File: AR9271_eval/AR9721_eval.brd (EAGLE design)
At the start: 160 x 100 mm, 125 parts, among them J1 UJ2-MIBH2-4-SMT-TR, J3 HTST-110-01-XX-DV, J7 132134-15, J8 132134-15, U1 U-ATHEROS-AR9271, U2 AT24C04C-XHM-T, U3 LT3080EQPBF, U4 LT3080EQPBF, U5 LT3080EQPBF, U6 LT3080EQPBF, Y1 ECS-400-10-36-CKY-TR

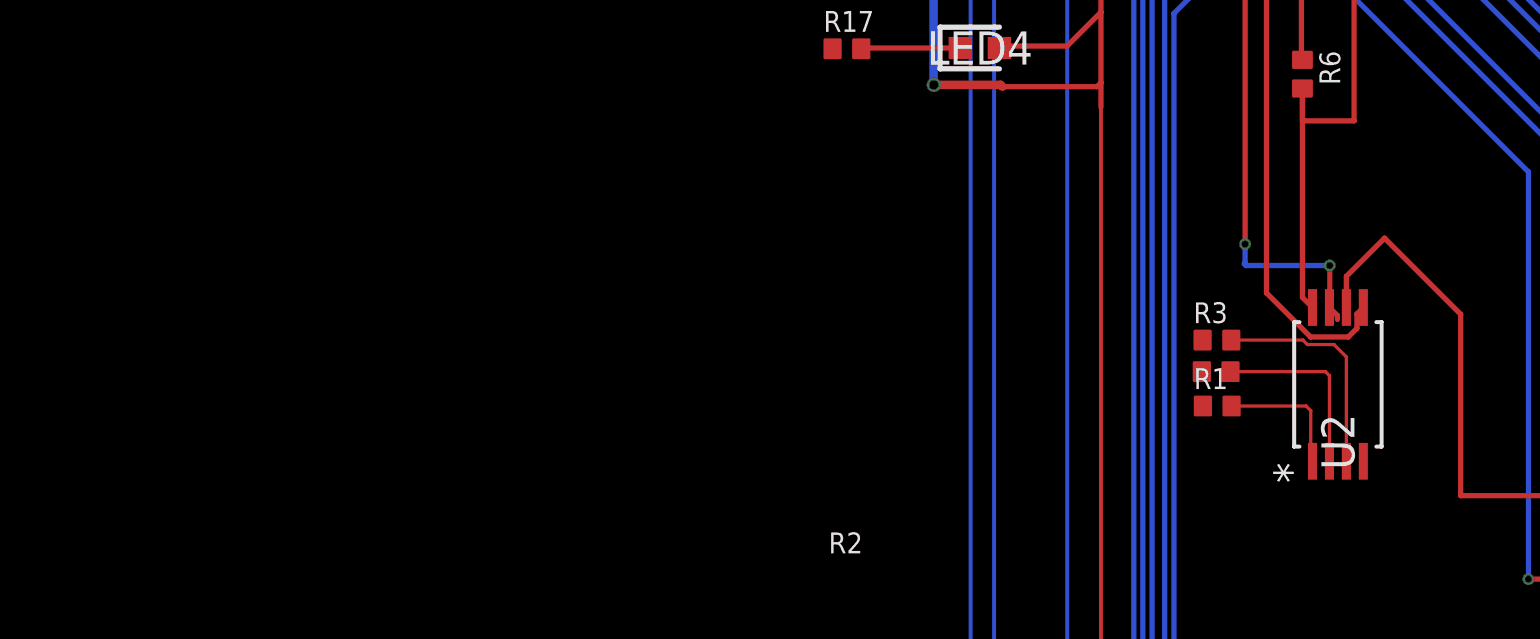
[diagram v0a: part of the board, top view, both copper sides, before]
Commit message: BRD and SCH now back in sync
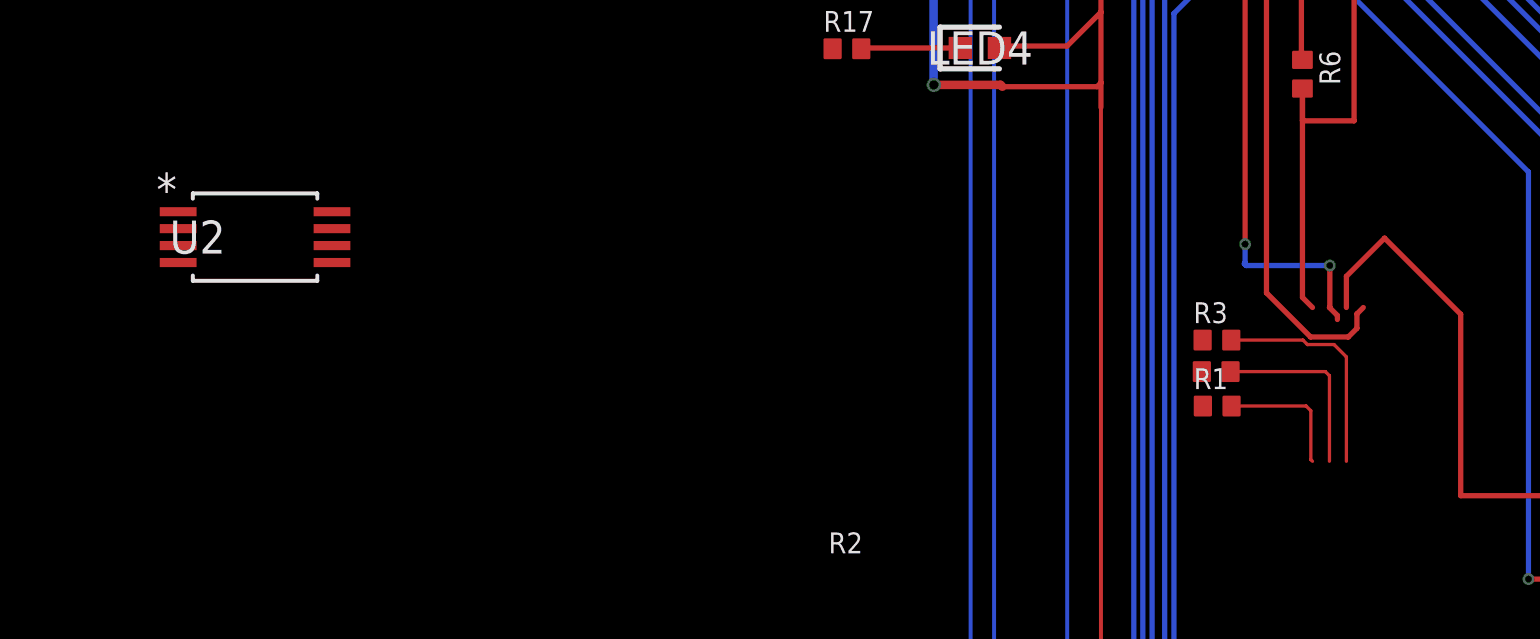
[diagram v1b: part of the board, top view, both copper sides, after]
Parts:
- U2: device AT24C04_TSSOP:8X -> U-Generic-AT24C04-EEPROM-I2C-4Kb-TSSOP:8X
- moved U2 41.9 mm to (44.1, 30.4), turned to 0 degrees

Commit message: Add files via upload
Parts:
- moved C39 99.7 mm to (32.0, 28.9)
- moved C27 96.9 mm to (24.7, 30.5)
- moved C28 92.2 mm to (25.8, 30.4)
- moved C37 86.3 mm to (22.2, 33.8), turned to 180 degrees
- moved C38 83.1 mm to (26.8, 28.8), turned to 180 degrees
- moved C36 80.9 mm to (22.2, 35.6), turned to 180 degrees
- moved C29 78.7 mm to (36.6, 29.3)
- moved C35 75.7 mm to (24.2, 44.4), turned to 180 degrees
- moved C33 75.1 mm to (24.2, 43.4), turned to 180 degrees
- moved C30 73.0 mm to (38.2, 29.3)
- moved C34 73.0 mm to (26.7, 43.3), turned to 180 degrees
- moved C40 66.2 mm to (43.0, 37.0)
- moved C50 61.5 mm to (63.7, 57.4)
- moved C41 60.7 mm to (29.1, 44.3)
- moved C31 60.5 mm to (42.1, 40.2), turned to 90 degrees
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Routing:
- net 3V3_D: track 202.7 -> 101.1 mm, vias 22 -> 15
- net LDO_IN: track 141.5 -> 90.0 mm, vias 11 -> 6
- net 1V2_A: track 91.9 -> 41.2 mm, vias 5 -> 3
- net N$25: track 53.2 -> 21.0 mm, vias 2 -> 0
- net N$3: track 57.8 -> 32.4 mm
- net GPIO11: track 114.3 -> 94.0 mm
- net N$23: track 23.2 -> 3.28 mm, vias 3 -> 0
- net RST_L: track 57.8 -> 41.0 mm
- net GPIO6: track 95.5 -> 78.8 mm
- net GPIO8: track 99.5 -> 82.7 mm
- net GPIO7: track 97.5 -> 80.7 mm
- net SWCOM1: track 55.9 -> 39.6 mm
- net GPIO5: track 93.7 -> 77.7 mm, vias 3 -> 2
- net SWCOM0: track 61.1 -> 45.1 mm
- net SWCOM2: track 60.7 -> 46.0 mm
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- removed copper zone on layer 15, net N$23
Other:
- board size 160 x 100 mm -> 105.7 x 84.6 mm

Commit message: Add files via upload
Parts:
- moved C46 28.8 mm to (61.8, 56.1)
- moved LED1 28.7 mm to (2.04, 7.56), turned to 270 degrees
- moved R34 28.6 mm to (55.2, 55.2)
- moved C22 28.4 mm to (15.4, 55.7)
- moved U4 28.4 mm to (58.5, 72.4)
- moved U6 28.4 mm to (44.5, 72.0)
- moved C23 28.4 mm to (12.3, 59.8)
- moved C47 28.4 mm to (30.6, 55.5)
- moved C48 28.4 mm to (28.0, 58.1)
- moved R33 28.4 mm to (25.5, 55.5)
- moved U5 28.4 mm to (30.6, 72.0)
- moved C1 28.4 mm to (33.1, 55.6)
- moved C24 28.4 mm to (19.2, 54.8)
- moved C49 28.4 mm to (48.3, 57.0)
- moved R27 28.4 mm to (12.3, 61.0)
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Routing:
- net LDO_IN: track 90.0 -> 122.6 mm, vias 6 -> 23
- net 1V2_D: track 90.0 -> 66.1 mm, vias 2 -> 12
- net USB_DM: track 83.4 -> 62.8 mm
- net N$32: track 5.22 -> 22.4 mm
- net N$25: track 21.0 -> 4.03 mm
- net 1V2_A: track 41.2 -> 24.9 mm, vias 3 -> 12
- net TDO: track 16.9 -> 32.4 mm
- net TCK: track 45.9 -> 60.9 mm
- net TDI: track 36.7 -> 51.6 mm
- net TMS: track 34.9 -> 48.8 mm
- net RST_L: track 41.0 -> 54.4 mm
- net 3V3_D: track 101.1 -> 114.1 mm, vias 15 -> 20
- net N$47: track 26.2 -> 14.2 mm, vias 4 -> 6
- net RCV_IN: track 5.29 -> 16.4 mm
- net N$37: track 22.0 -> 13.5 mm, vias 3 -> 9
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- added copper zone on layer 16, net GND
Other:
- board size 105.7 x 84.6 mm -> 98.9 x 78.9 mm

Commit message: Add files via upload
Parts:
- moved J4 5.20 mm to (86.1, 3.21)
- moved J6 5.20 mm to (82.3, 3.21)
- moved LED10 5.20 mm to (74.7, 8.29)
- moved LED11 5.20 mm to (77.2, 8.30)
- moved LED12 5.20 mm to (79.7, 8.29)
- moved LED6 5.20 mm to (64.5, 8.29)
- moved LED8 5.20 mm to (69.6, 8.28)
- moved R19 5.20 mm to (64.5, 12.1)
- moved R21 5.20 mm to (69.6, 12.1)
- moved R23 5.20 mm to (74.7, 12.1)
- moved R24 5.20 mm to (77.2, 12.1)
- moved R25 5.20 mm to (79.7, 12.1)
- moved LED5 5.20 mm to (62.0, 8.29)
- moved R18 5.20 mm to (62.0, 12.1)
- moved LED7 5.20 mm to (67.0, 8.29)
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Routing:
- net GPIO9: track 79.7 -> 74.5 mm
- net GPIO8: track 78.7 -> 73.5 mm
- net GPIO13: track 71.7 -> 66.5 mm
- net GPIO10: track 76.7 -> 71.5 mm
- net GPIO14: track 65.1 -> 59.9 mm
- net GPIO7: track 76.7 -> 71.5 mm
- net GPIO6: track 74.8 -> 69.6 mm
- net GPIO5: track 73.7 -> 68.5 mm
- net GPIO15: track 74.9 -> 69.7 mm
- net GPIO11: track 89.6 -> 84.4 mm
- net 3V3_A: track 63.9 -> 58.8 mm, vias 11 -> 10
- net TDO: track 32.4 -> 28.4 mm
- net USB_DM: track 62.8 -> 58.9 mm
- net USB_DP: track 68.3 -> 64.4 mm
- net LDO_IN: track 122.6 -> 118.7 mm
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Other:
- board size 98.9 x 78.9 mm -> 94.2 x 78.9 mm

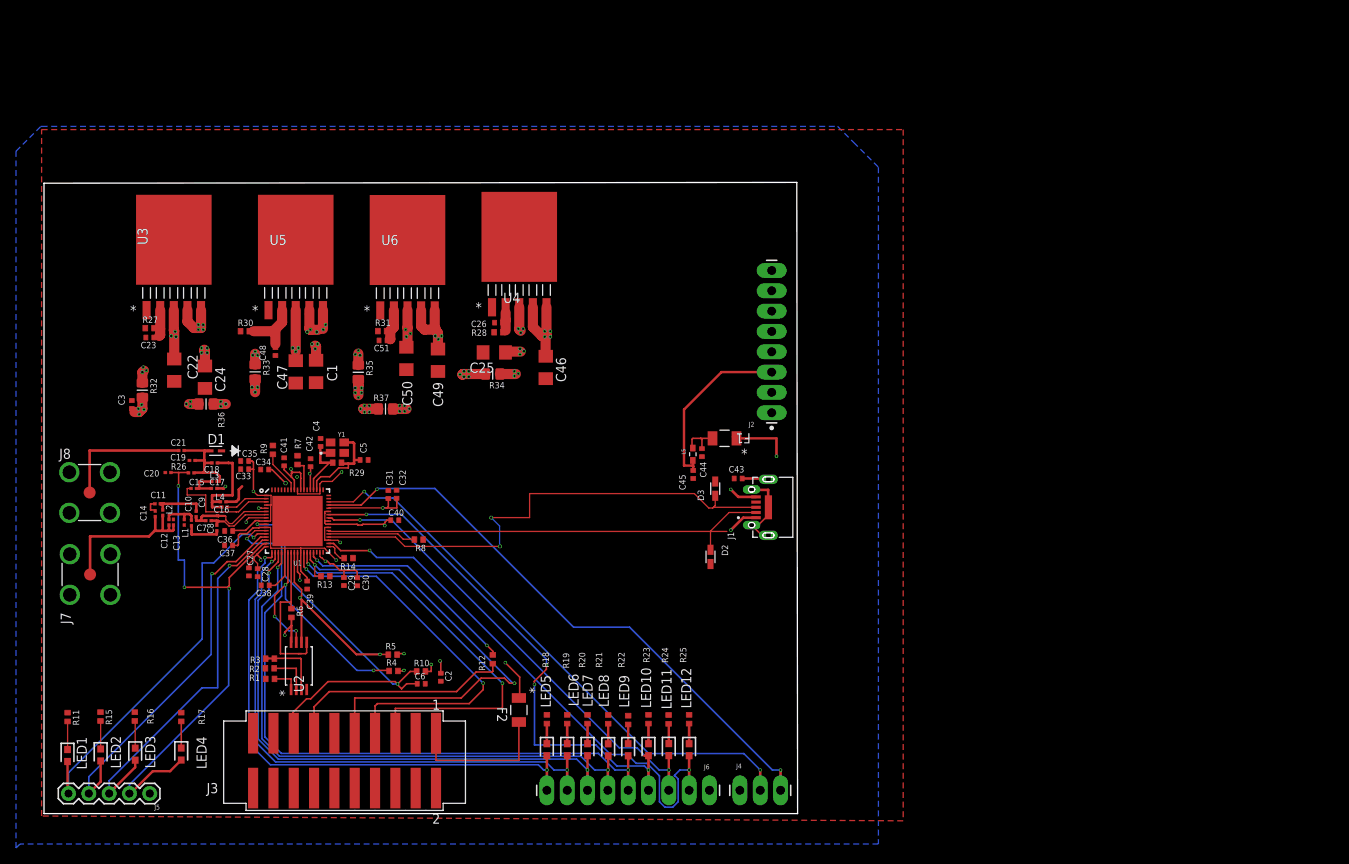
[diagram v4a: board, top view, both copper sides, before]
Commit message: Beginning of OCD cleanup; started with USB lines, worked on RF layout grouping, moved to power planes.
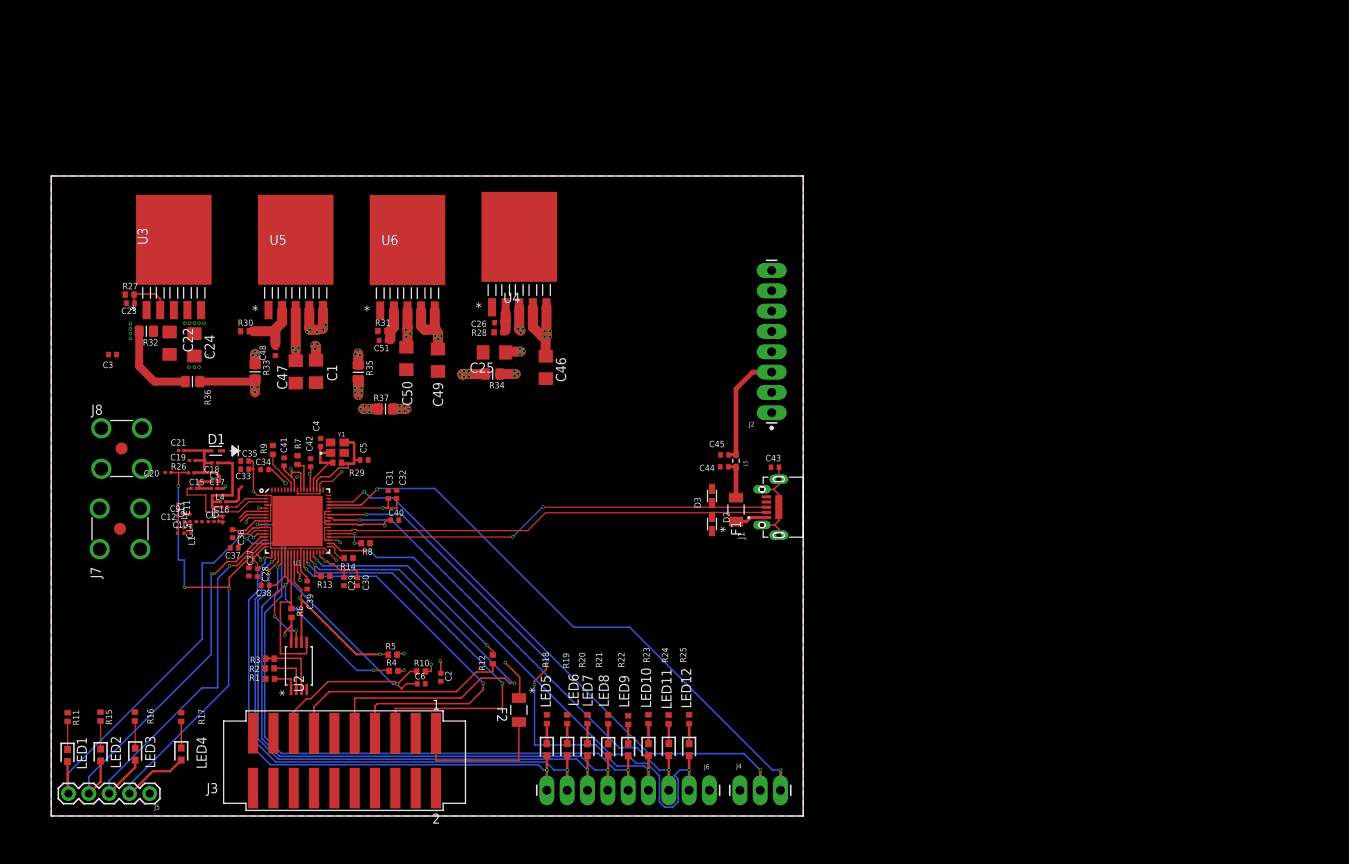
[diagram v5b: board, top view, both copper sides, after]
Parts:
- moved F1 9.02 mm to (85.6, 38.3), turned to 90 degrees
- moved R32 7.39 mm to (11.9, 60.6), turned to 180 degrees
- moved J7 6.83 mm to (8.60, 35.9)
- moved J8 6.80 mm to (8.80, 45.9)
- moved C3 6.70 mm to (7.67, 57.7), turned to 180 degrees
- moved R8 6.67 mm to (39.3, 34.1), turned to 180 degrees
- moved L5 5.46 mm to (85.6, 44.4), turned to 90 degrees
- moved C23 4.93 mm to (9.90, 64.1)
- moved R27 4.89 mm to (9.81, 65.2)
- moved C43 4.81 mm to (90.5, 43.6)
- moved C45 4.64 mm to (84.2, 45.1), turned to 180 degrees
- moved C24 4.26 mm to (17.9, 58.9)
- moved D2 4.12 mm to (82.6, 36.5)
- moved C14 3.47 mm to (15.8, 35.7), turned to 270 degrees
- moved C22 3.42 mm to (14.8, 59.1)
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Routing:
- net LDO_IN: track 118.7 -> 51.2 mm, vias 23 -> 20
- net XMIT_OUT: track 20.6 -> 0.00 mm
- net USB_+V: track 23.2 -> 4.01 mm, vias 2 -> 0
- net 3V3_D: track 114.8 -> 95.8 mm, vias 20 -> 17
- net RCV_IN: track 16.4 -> 0.03 mm
- net N$33: track 15.6 -> 0.00 mm, vias 6 -> 0
- net RFOUT_N: track 12.0 -> 3.69 mm
- net USB+5V: track 22.6 -> 14.5 mm
- net USB_DP: track 64.4 -> 57.3 mm
- net N$18: track 6.66 -> 0.00 mm
- net N$2: track 11.0 -> 5.27 mm, vias 0 -> 2
- net 3V3_A: track 58.8 -> 64.4 mm, vias 10 -> 7
- net GND: track 11.4 -> 6.01 mm, vias 2 -> 5
- net N$14: track 4.82 -> 0.00 mm
- net N$22: track 4.70 -> 0.00 mm
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- added copper zone on layer 1, net RFOUT_N
- removed copper zone on layer 15, net 3V3_A
- removed copper zone on layer 1, net RFOUT_P1
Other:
- board size 94.2 x 78.9 mm -> 94 x 80 mm

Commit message: Here's my newest update to the AR9721 board
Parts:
- moved R36 7.76 mm to (23.8, 49.6)
- moved R32 7.37 mm to (14.2, 53.6), turned to 270 degrees
- moved C3 6.80 mm to (10.7, 51.6)
- moved C22 6.60 mm to (16.4, 52.7)
- moved C19 6.52 mm to (21.2, 39.0), turned to 270 degrees
- moved R27 6.49 mm to (10.9, 58.8)
- moved U5 6.49 mm to (31.7, 65.6)
- moved U6 6.49 mm to (45.6, 65.6)
- moved U3 6.49 mm to (16.4, 65.6)
- moved C24 6.49 mm to (19.0, 52.5)
- moved C23 6.49 mm to (11.0, 57.7)
- moved U4 6.49 mm to (59.6, 66.0)
- moved C20 6.46 mm to (19.7, 39.0), turned to 270 degrees
- moved C25 6.38 mm to (59.6, 53.1), turned to 270 degrees
- moved R16 6.30 mm to (16.4, 10.2)
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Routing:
- net LDO_IN: track 51.2 -> 12.1 mm
- net 3V3_D: track 95.8 -> 70.7 mm, vias 17 -> 19
- net N$43: track 14.6 -> 0.00 mm
- net N$47: track 14.2 -> 0.00 mm, vias 6 -> 0
- net N$37: track 13.5 -> 0.00 mm, vias 9 -> 0
- net N$44: track 13.0 -> 0.00 mm, vias 6 -> 0
- net N$4: track 38.6 -> 25.8 mm, vias 2 -> 0
- net 3V3_A: track 64.4 -> 52.1 mm, vias 7 -> 10
- net RCV_IN: track 0.03 -> 10.3 mm
- net N$17: track 12.1 -> 1.80 mm
- net RFIN_P: track 13.8 -> 3.87 mm
- net N$24: track 12.8 -> 4.43 mm
- net XMIT_OUT: track 0.00 -> 7.99 mm
- net SWCOM3: track 69.9 -> 63.1 mm
- net 1V2_A: track 28.0 -> 21.8 mm, vias 12 -> 8
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- added copper zone on layer 15, net 3V3_A
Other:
- board size 94 x 80 mm -> 88.1 x 72.7 mm
